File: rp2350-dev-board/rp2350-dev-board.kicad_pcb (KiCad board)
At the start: 2 copper layers, 40 parts, among them J1 USB_C_Receptacle_USB2.0_14P, J2 Conn_02x10_Odd_Even, J3 HDMI_A, SW1 BOOT SELECTOR, SW2 RST, U1 RP2350_60QFN, U2 AMS1117-3.3, U3 W25Q16JVSS, Y1 12Mhz HC49-SD

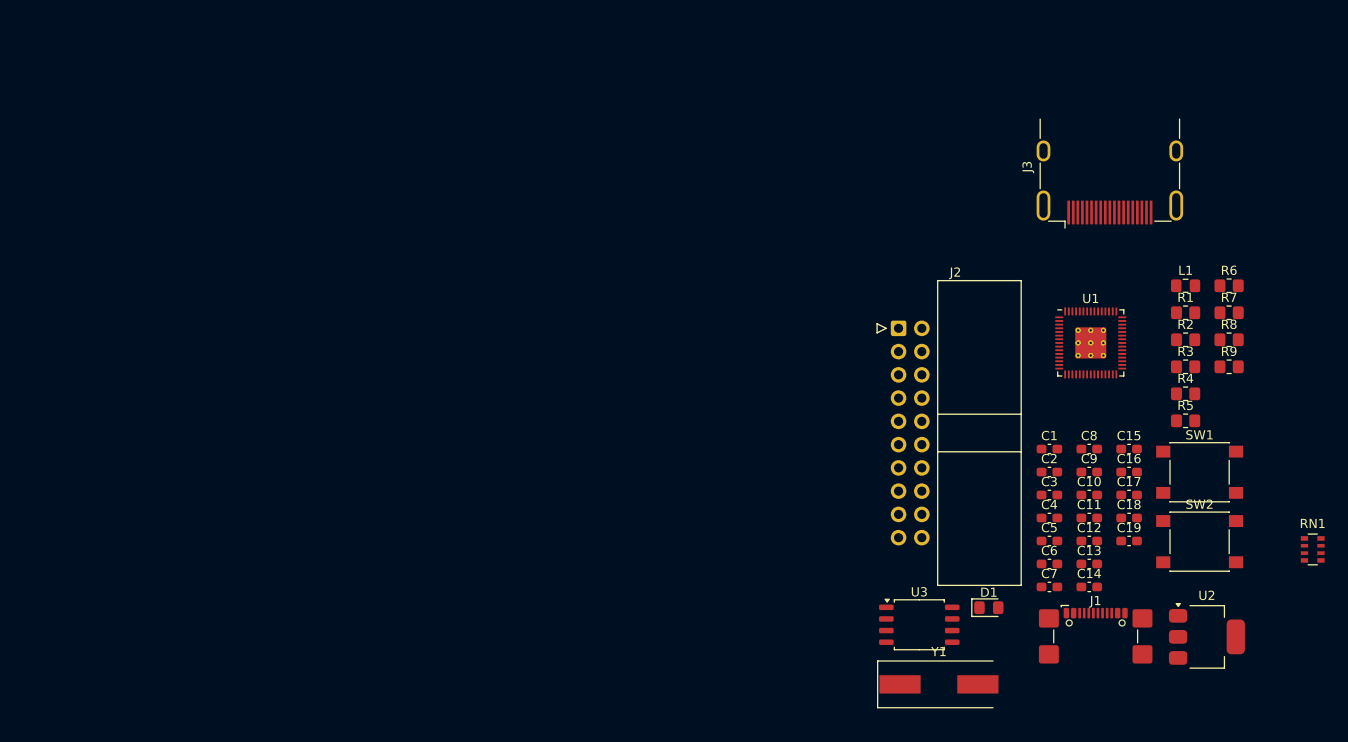
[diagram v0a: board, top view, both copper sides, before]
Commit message: feat: finish rp2350-dev-board schematic
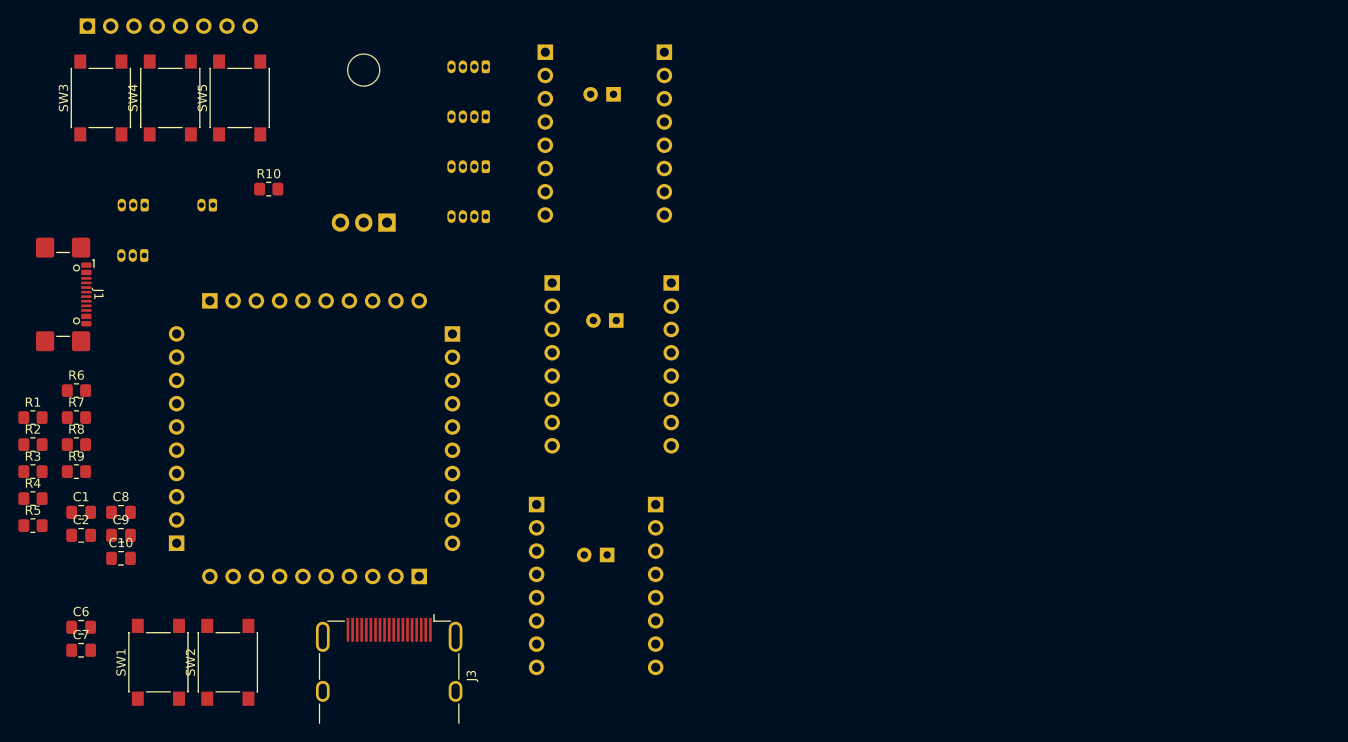
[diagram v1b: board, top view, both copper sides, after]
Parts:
- removed C11, C12, C16: 100nF, Capacitor_SMD:C_0603_1608Metric_Pad1.08x0.95mm_HandSolder
- removed C13: 2u2F, Capacitor_SMD:C_0603_1608Metric_Pad1.08x0.95mm_HandSolder
- removed C14, C15: 12pF, Capacitor_SMD:C_0603_1608Metric_Pad1.08x0.95mm_HandSolder
- removed C17, C18, C19: 4.7uF, Capacitor_SMD:C_0603_1608Metric_Pad1.08x0.95mm_HandSolder
- removed D1: red, LED_SMD:LED_0805_2012Metric_Pad1.15x1.40mm_HandSolder
- removed L1: L, Inductor_SMD:L_0805_2012Metric_Pad1.15x1.40mm_HandSolder
- removed RN1: R_Pack04, Resistor_SMD:R_Array_Convex_4x0603
- removed Y1: 12Mhz HC49-SD, Crystal:Crystal_SMD_HC49-SD
- added J10: M1, Connector_Hirose:Hirose_DF13-04P-1.25DSA_1x04_P1.25mm_Vertical, B.Cu at (136.4, 77.9)
- added J11: M1, Connector_Hirose:Hirose_DF13-04P-1.25DSA_1x04_P1.25mm_Vertical, B.Cu at (136.4, 83.3)
- added J12: M1, Connector_Hirose:Hirose_DF13-04P-1.25DSA_1x04_P1.25mm_Vertical, B.Cu at (136.4, 88.8)
- added J13: PWR_IN, Connector_Hirose:Hirose_DF13-02P-1.25DSA_1x02_P1.25mm_Vertical, B.Cu at (106.6, 93.0)
- added J14: SWD, Connector_Hirose:Hirose_DF13-04P-1.25DSA_1x04_P1.25mm_Vertical, B.Cu at (136.4, 94.2)
- added J8: 1.47_IPS_LCD, Connector_PinHeader_2.54mm:PinHeader_1x08_P2.54mm_Vertical, B.Cu at (92.9, 73.5)
- added J9: TMC_Volt_Select, Connector_Hirose:Hirose_DF13-03P-1.25DSA_1x03_P1.25mm_Vertical, B.Cu at (99.2, 93.0)
- added R10: 2K, Resistor_SMD:R_0805_2012Metric_Pad1.20x1.40mm_HandSolder, F.Cu at (112.7, 91.2)
- added SW3: BTN1, Button_Switch_SMD:SW_Push_1P1T_NO_6x6mm_H9.5mm, F.Cu at (94.4, 81.3)
- added SW4: BTN1, Button_Switch_SMD:SW_Push_1P1T_NO_6x6mm_H9.5mm, F.Cu at (101.9, 81.3)
- added SW5: BTN1, Button_Switch_SMD:SW_Push_1P1T_NO_6x6mm_H9.5mm, F.Cu at (109.5, 81.3)
- added U4: L7805, Package_TO_SOT_THT:TO-220-3_Horizontal_TabDown, B.Cu at (125.6, 94.9)
- added U5: ~, rp2350-tempel-lib:RP2350_Tempel_Footprint, B.Cu at (120.9, 137.7)
- C1, C2: value 22uF -> 100nF; footprint Capacitor_SMD:C_0603_1608Metric_Pad1.08x0.95mm_HandSolder -> Capacitor_SMD:C_0805_2012Metric_Pad1.18x1.45mm_HandSolder
- C10, C6, C7, C8, C9: footprint Capacitor_SMD:C_0603_1608Metric_Pad1.08x0.95mm_HandSolder -> Capacitor_SMD:C_0805_2012Metric_Pad1.18x1.45mm_HandSolder
- C3: value 1uF -> 100uF; footprint Capacitor_SMD:C_0603_1608Metric_Pad1.08x0.95mm_HandSolder -> Capacitor_THT:CP_Radial_D6.3mm_P2.50mm; moved to B.Cu
- C4: value 4.7uF -> 100uF; footprint Capacitor_SMD:C_0603_1608Metric_Pad1.08x0.95mm_HandSolder -> Capacitor_THT:CP_Radial_D6.3mm_P2.50mm; moved to B.Cu
- C5: value 100nF -> 100uF; footprint Capacitor_SMD:C_0603_1608Metric_Pad1.08x0.95mm_HandSolder -> Capacitor_THT:CP_Radial_D6.3mm_P2.50mm; moved to B.Cu
- J2: value Conn_02x10_Odd_Even -> M_EN; footprint Connector_IDC:IDC-Header_2x10_P2.54mm_Horizontal -> Connector_Hirose:Hirose_DF13-03P-1.25DSA_1x03_P1.25mm_Vertical; moved to B.Cu
- R6, R8: value 1K -> 2K
- R7: value 2K2 -> 2K
- R9: value 33 -> 2K
- SW1: value BOOT SELECTOR -> BTN1
- SW2: value RST -> BTN1
- U1: value RP2350_60QFN -> ~; footprint lib:RP2350-QFN-60-1EP_7x7_P0.4mm_EP3.4x3.4mm_ThermalVias -> rp2350-tempel-lib:TMC2209_MKS_V2; moved to B.Cu
- U2: value AMS1117-3.3 -> ~; footprint Package_TO_SOT_SMD:SOT-223-3_TabPin2 -> rp2350-tempel-lib:TMC2209_MKS_V2; moved to B.Cu
- U3: value W25Q16JVSS -> ~; footprint Package_SO:SOIC-8_5.23x5.23mm_P1.27mm -> rp2350-tempel-lib:TMC2209_MKS_V2; moved to B.Cu
- moved R1 126.4 mm to (87.0, 116.2)
- moved R2 126.4 mm to (87.0, 119.2)
- moved R3 126.4 mm to (87.0, 122.1)
- moved R4 126.4 mm to (87.0, 125.0)
- moved R5 126.4 mm to (87.0, 128.0)
- moved R6 126.4 mm to (91.7, 113.2)
- moved R7 126.4 mm to (91.7, 116.2)
- moved R8 126.4 mm to (91.7, 119.2)
- moved R9 126.4 mm to (91.7, 122.1)
- moved J1 120.2 mm to (89.1, 102.8), turned to -90 degrees
- moved SW1 115.6 mm to (100.7, 142.9), turned to 90 degrees
- moved SW2 106.9 mm to (108.2, 142.9), turned to 90 degrees
- moved C10 106.0 mm to (96.6, 131.6)
- moved C8 106.0 mm to (96.6, 126.5)
- moved C9 106.0 mm to (96.6, 129.1)
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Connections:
- C1 pad 1: +5V -> VS
- C10 pad 1: +3.3V -> /GPIO26_ADC0
- C2 pad 1: +3.3V -> +5V
- C3 pad 1: +1V1 -> VS
- C4 pad 1: +1V1 -> VS
- C5 pad 1: +1V1 -> VS
- C6 pad 1: +3.3V -> /GPIO22
- C7 pad 1: +3.3V -> /GPIO23
- C8 pad 1: +3.3V -> /GPIO24
- C9 pad 1: +3.3V -> /GPIO25
- J1 pad S1: GND -> unconnected-(J1-SHIELD-PadS1)_2
- J2 pad 1: unconnected-(J2-Pin_1-Pad1) -> +3.3V
- J2 pad 2: unconnected-(J2-Pin_2-Pad2) -> /M_EN
- J2 pad 3: unconnected-(J2-Pin_3-Pad3) -> GND
- J3 pad 1: /HSTX5 -> /GPIO16
- J3 pad 10: /HSTX3 -> /GPIO14
- J3 pad 12: /HSTX4 -> /GPIO15
- J3 pad 15: unconnected-(J3-SCL-Pad15) -> /GPIO5
- J3 pad 16: unconnected-(J3-SDA-Pad16) -> /GPIO4
- J3 pad 17: unconnected-(J3-GND-Pad17) -> GND
- J3 pad 18: unconnected-(J3-+5V-Pad18) -> +5V
- J3 pad 3: /HSTX6 -> /GPIO17
- J3 pad 4: /HSTX7 -> /GPIO18
- J3 pad 6: /HSTX8 -> /GPIO19
- J3 pad 7: /HSTX1 -> /GPIO12
- J3 pad 9: /HSTX2 -> /GPIO13
- R5 pad 1: Net-(D1-K) -> /GPIO20
- R5 pad 2: GND -> /GPIO21
- R6 pad 1: Net-(C15-Pad1) -> /GPIO22
- R6 pad 2: /XOUT -> +3.3V
- R7 pad 1: /SPI_SS_N -> /GPIO23
- R7 pad 2: Net-(R7-Pad2) -> +3.3V
- R8 pad 1: Net-(R8-Pad1) -> /GPIO24
- R8 pad 2: Net-(U1-RUN) -> +3.3V
- R9 pad 1: +3.3V -> /GPIO25
- R9 pad 2: Net-(U1-VREG_AVDD) -> +3.3V
- SW1 pad 1: Net-(R7-Pad2) -> /GPIO22
- SW2 pad 1: Net-(R8-Pad1) -> /GPIO23
- U1 pad 1: +3.3V -> GND
- U1 pad 10: /GPIO7 -> GND
- U1 pad 11: +3.3V -> GND
- U1 pad 12: /GPIO8 -> unconnected-(U1-r8-Pad12)
- U1 pad 13: /GPIO9 -> /GPIO20
- U1 pad 14: /GPIO10 -> (no net)
- U1 pad 15: /GPIO11 -> unconnected-(U1-STEP-Pad15)
- U1 pad 16: /HSTX1 -> unconnected-(U1-DIR-Pad16)
- U1 pad 2: /GPIO0 -> VDD
- U1 pad 3: /GPIO1 -> Net-(J10-Pin_1)
- U1 pad 4: /GPIO2 -> Net-(J10-Pin_2)
- U1 pad 5: /GPIO3 -> Net-(J10-Pin_3)
- U1 pad 6: +1V1 -> Net-(J10-Pin_4)
- U1 pad 7: /GPIO4 -> (no net)
- U1 pad 8: /GPIO5 -> VS
- U1 pad 9: /GPIO6 -> /M_EN
- U2 pad 2: +3.3V -> VDD
- U2 pad 3: +5V -> Net-(J11-Pin_1)
- U3 pad 1: /SPI_SS_N -> GND
- U3 pad 2: /SPI_SD1 -> VDD
- U3 pad 3: /SPI_SD2 -> Net-(J12-Pin_1)
- U3 pad 4: GND -> Net-(J12-Pin_2)
- U3 pad 5: /SPI_SD0 -> Net-(J12-Pin_3)
- U3 pad 6: /SPI_SCLK -> Net-(J12-Pin_4)
- U3 pad 7: /SPI_SD3 -> (no net)
- U3 pad 8: +3.3V -> VS

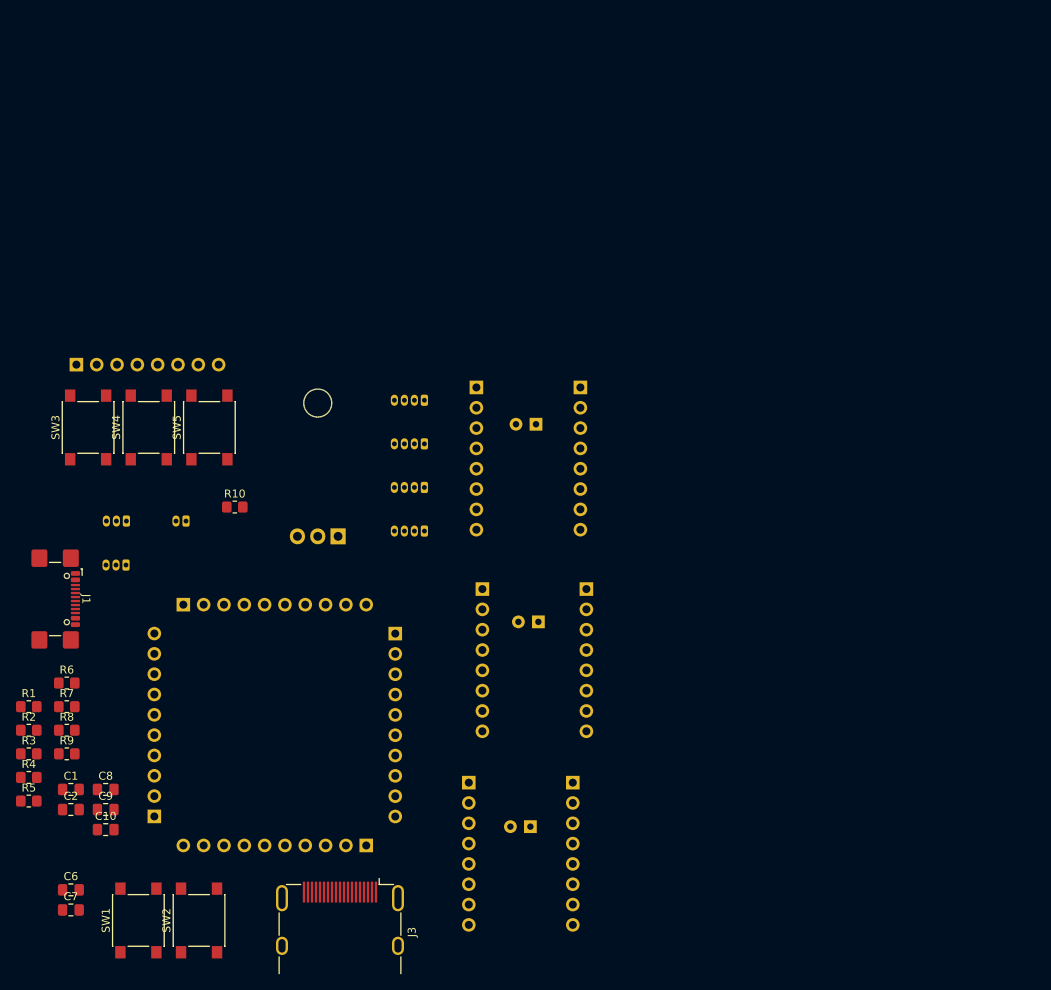
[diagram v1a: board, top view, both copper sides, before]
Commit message: feat: progress on routing tempel rp2350a dev board
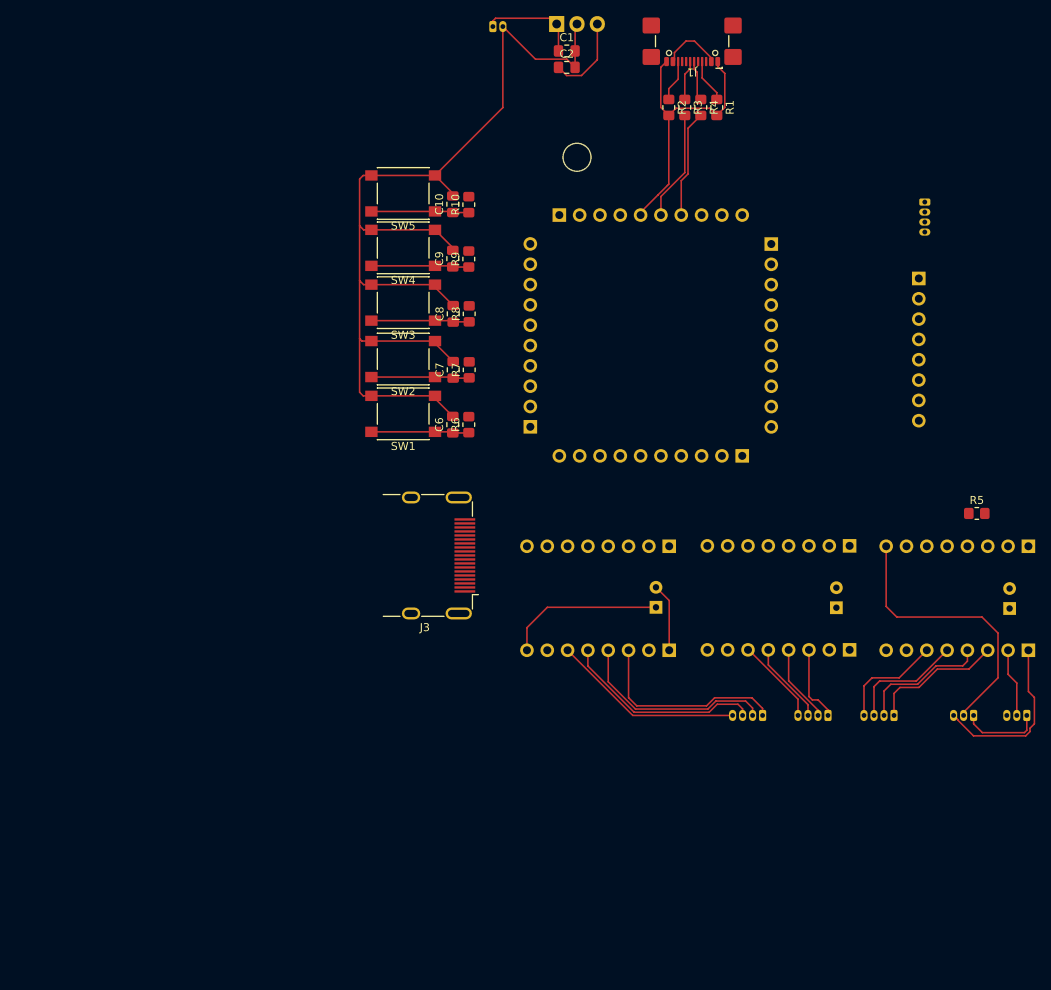
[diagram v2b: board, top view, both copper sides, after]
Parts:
- moved R5 123.8 mm to (205.5, 92.1)
- moved R4 118.6 mm to (170.9, 41.3), turned to -90 degrees
- moved J9 115.1 mm to (211.7, 117.3)
- moved R3 115.1 mm to (168.9, 41.3), turned to -90 degrees
- moved R1 114.0 mm to (172.9, 41.3), turned to -90 degrees
- moved R2 111.6 mm to (166.9, 41.3), turned to -90 degrees
- moved C2 111.6 mm to (154.2, 36.3)
- moved C1 111.2 mm to (154.2, 34.2)
- moved J2 107.6 mm to (205.1, 117.3)
- moved J1 107.5 mm to (169.9, 31.9), turned to 180 degrees
- moved J8 105.8 mm to (198.2, 62.7), turned to 180 degrees
- moved C10 89.4 mm to (140.0, 53.4), turned to 90 degrees
- moved C7 82.7 mm to (140.0, 74.1), turned to 90 degrees
- moved C9 81.4 mm to (140.0, 60.2), turned to 90 degrees
- moved R9 79.7 mm to (142.0, 60.2), turned to 90 degrees
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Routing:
- net GND: track 0.00 -> 196.7 mm
- net /M_EN: track 0.00 -> 35.0 mm
- net VS: track 0.00 -> 32.6 mm
- net Net-(J12-Pin_3): track 0.00 -> 25.2 mm
- net Net-(J12-Pin_2): track 0.00 -> 25.1 mm
- net Net-(J12-Pin_1): track 0.00 -> 24.9 mm
- net Net-(J12-Pin_4): track 0.00 -> 24.0 mm
- net +5V: track 0.00 -> 18.3 mm
- net Net-(J10-Pin_1): track 0.00 -> 16.7 mm
- net Net-(J10-Pin_2): track 0.00 -> 16.4 mm
- net Net-(J10-Pin_3): track 0.00 -> 14.6 mm
- net /USB_DM: track 0.00 -> 13.7 mm
- net /USB_DP: track 0.00 -> 13.5 mm
- net Net-(J10-Pin_4): track 0.00 -> 13.4 mm
- net /GPIO24: track 0.00 -> 12.3 mm
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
